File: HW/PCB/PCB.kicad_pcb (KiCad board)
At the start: 2 copper layers, 104.5 x 67 mm, 68 parts, among them J1 USB4105-GF-A, J4 Micro_SD_Card_Det_Hirose_DM3AT, Q2 SI1308EDL-T1-GE3, SW1 ssss213202, SW2 SKRPACE010, SW3 SKRPACE010, SW4 SKRPACE010, U1 BME280, U2 E-Paper 4.26inch, 800x480, U4 ESP32-S3-WROOM-1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

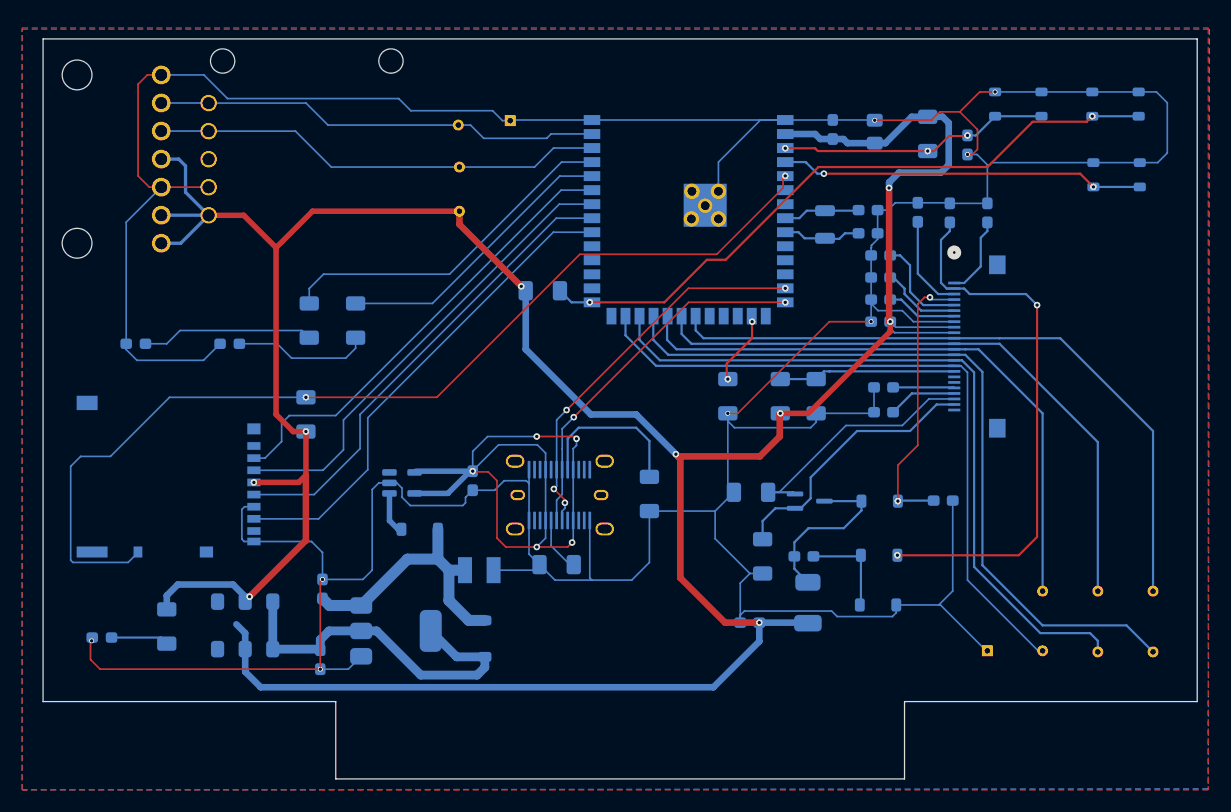
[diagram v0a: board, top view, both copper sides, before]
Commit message: change PCD layout
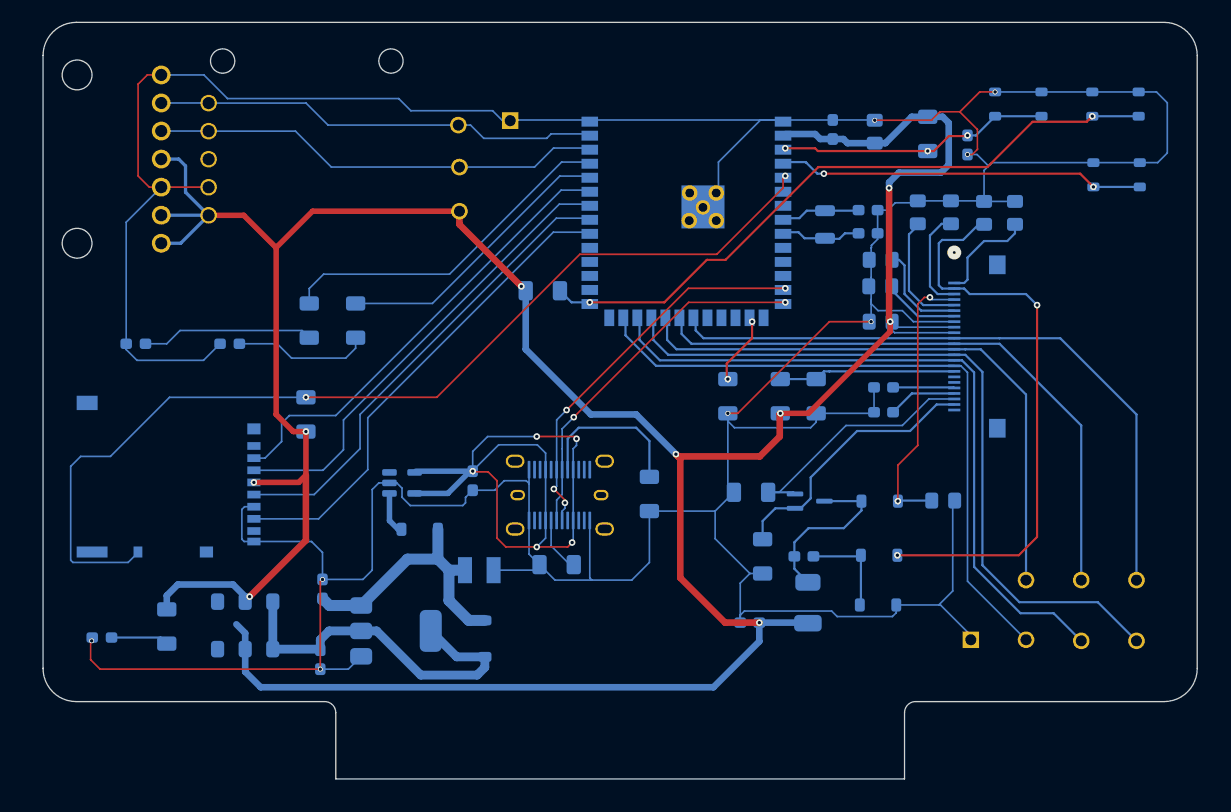
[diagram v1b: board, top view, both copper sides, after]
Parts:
- removed U4: ESP32-S3-WROOM-1, mylib:ESP32-S3-WROOM-1
- added U3: ESP32-S3-WROOM-1, mylib:ESP32-S3-WROOM-1, B.Cu at (146.8, 59.8)
- C10, C17, C22, C9: footprint Capacitor_SMD:C_0603_1608Metric_Pad1.08x0.95mm_HandSolder -> Capacitor_SMD:C_0805_2012Metric_Pad1.18x1.45mm_HandSolder
- C12: footprint TAJ_SMD:TAJB_AVX -> mylib:TAJB_AVX
- C13, C15, C16, C20: value 4.7uF -> 1uF; footprint Capacitor_SMD:C_0603_1608Metric_Pad1.08x0.95mm_HandSolder -> Capacitor_SMD:C_0805_2012Metric_Pad1.18x1.45mm_HandSolder
- U2: footprint XF2M-2415-1A:CONN_XF2M-2415-1A_OMR -> mylib:CONN_XF2M-2415-1A_OMR
- moved C13 5.15 mm to (167.7, 62.7), turned to -90 degrees
- moved C16 3.10 mm to (173.7, 62.8)
- moved C15 3.00 mm to (170.7, 62.7)
- moved C17 2.50 mm to (176.5, 62.8)
- moved TP1 1.80 mm to (172.5, 101.4)
- moved TP2 1.80 mm to (177.5, 101.4)
- moved TP3 1.80 mm to (182.5, 101.5)
- moved TP4 1.80 mm to (187.5, 101.5)
- moved TP5 1.80 mm to (177.5, 96.0)
- moved TP6 1.80 mm to (182.5, 96.0)
- moved TP7 1.80 mm to (187.5, 96.0)
- moved C22 1.60 mm to (164.3, 67.0)
- moved C10 1.20 mm to (164.3, 69.4)
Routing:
- net EPAPER_PREVGL: track 49.7 -> 52.6 mm
- net ESP32_IO47_EPAPER_RST: track 66.2 -> 63.7 mm
- net Net-(U2-VCOM): track 7.26 -> 9.35 mm
- net Net-(U2-VSH): track 9.07 -> 11.0 mm
- net ESP32_IO21_EPAPER_DC: track 69.4 -> 67.4 mm
- net Net-(U2-VPP): track 7.34 -> 9.05 mm
- net ESP32_IO13_EPAPER_SCK: track 56.9 -> 55.2 mm
- net ESP32_IO12_EPAPER_MOSI: track 61.0 -> 59.4 mm
- net ESP32_IO14_EPAPER_CS: track 55.0 -> 53.5 mm
- net ESP32_IO48_EPAPER_BUSY: track 62.3 -> 60.9 mm
- net GND: track 421.3 -> 422.4 mm
- net Net-(U2-VSL): track 8.75 -> 9.43 mm
- net Net-(U2-VDD): track 6.42 -> 6.98 mm
- removed copper zone on B.Cu, net GND
- removed copper zone on F.Cu, net GND
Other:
- board size 104.5 x 67 mm -> 104.5 x 68.5 mm
